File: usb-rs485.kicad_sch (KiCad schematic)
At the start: 4 parts

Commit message: moved it elsewhere but MEH
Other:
- sheet RS485 Transceiver ports: added VLOGIC_MOTOR; removed none
- moved on the sheet: J2
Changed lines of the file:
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@@
+    (stroke (width 0) (type default))
+  )
+  (wire (pts (xy 324.485 145.415) (xy 324.485 146.685))
     (stroke (width 0) (type default))
   )
@@
     (stroke (width 0) (type default))
   )
-  (wire (pts (xy 328.93 154.94) (xy 328.93 155.575))
+  (wire (pts (xy 337.82 154.94) (xy 337.82 155.575))
     (stroke (width 0) (type default))
   )
@@
     (stroke (width 0) (type default))
   )
-  (wire (pts (xy 322.58 149.86) (xy 329.565 149.86))
+  (wire (pts (xy 322.58 149.86) (xy 338.455 149.86))
     (stroke (width 0) (type default))
   )
@@
     (stroke (width 0) (type default))
   )
-  (wire (pts (xy 328.93 147.32) (xy 329.565 147.32))
+  (wire (pts (xy 337.82 147.32) (xy 338.455 147.32))
     (stroke (width 0) (type default))
   )
@@
     (stroke (width 0) (type default))
   )
+  (wire (pts (xy 322.58 152.4) (xy 338.455 152.4))
+    (stroke (width 0) (type default))
+  )
   (wire (pts (xy 300.355 192.405) (xy 302.26 192.405))
     (stroke (width 0) (type default))
@@
     (stroke (width 0) (type default))
   )
-  (wire (pts (xy 322.58 152.4) (xy 329.565 152.4))
-    (stroke (width 0) (type default))
-  )
   (wire (pts (xy 279.4 149.86) (xy 299.085 149.86))
     (stroke (width 0) (type default))
@@
     (stroke (width 0) (type default))
   )
-  (wire (pts (xy 328.93 146.685) (xy 328.93 147.32))
-    (stroke (width 0) (type default))
-  )
-  (wire (pts (xy 328.93 154.94) (xy 329.565 154.94))
+  (wire (pts (xy 324.485 146.685) (xy 322.58 146.685))
+    (stroke (width 0) (type default))
+  )
+  (wire (pts (xy 337.82 146.685) (xy 337.82 147.32))
+    (stroke (width 0) (type default))
+  )
+  (wire (pts (xy 337.82 154.94) (xy 338.455 154.94))
     (stroke (width 0) (type default))
   )
@@
     (effects (font (size 1.27 1.27)) (justify right bottom))
   )
+  (label "6V0" (at 324.485 145.415 0) (fields_autoplaced)
+    (effects (font (size 1.27 1.27)) (justify left bottom))
+  )
   (label "RX" (at 287.02 149.86 0) (fields_autoplaced)
     (effects (font (size 1.27 1.27)) (justify left bottom))
   )
-  (label "VUSB" (at 328.93 146.685 180) (fields_autoplaced)
+  (label "VUSB" (at 337.82 146.685 180) (fields_autoplaced)
     (effects (font (size 1.27 1.27)) (justify right bottom))
   )
@@
     )
   )
-  (symbol (lib_id "power:GND") (at 328.93 155.575 0) (unit 1)
+  (symbol (lib_id "power:GND") (at 337.82 155.575 0) (unit 1)
     (in_bom yes) (on_board yes) (dnp no)
-    (property "Reference" "#PWR011" (at 328.93 161.925 0)
-      (effects (font (size 1.27 1.27)) hide)
-    )
-    (property "Value" "GND" (at 328.93 159.385 0)
-      (effects (font (size 1.27 1.27)))
-    )
-    (property "Footprint" "" (at 328.93 155.575 0)
-      (effects (font (size 1.27 1.27)) hide)
-    )
-    (property "Datasheet" "" (at 328.93 155.575 0)
+    (property "Reference" "#PWR011" (at 337.82 161.925 0)
+      (effects (font (size 1.27 1.27)) hide)
+    )
+    (property "Value" "GND" (at 337.82 159.385 0)
+      (effects (font (size 1.27 1.27)))
+    )
+    (property "Footprint" "" (at 337.82 155.575 0)
+      (effects (font (size 1.27 1.27)) hide)
+    )
+    (property "Datasheet" "" (at 337.82 155.575 0)
       (effects (font (size 1.27 1.27)) hide)
     )
@@
     )
   )
-  (symbol (lib_id "usb-rs485:ThruHoleX4") (at 332.105 151.13 0) (mirror y) (unit 1)
+  (symbol (lib_id "usb-rs485:ThruHoleX4") (at 340.995 151.13 0) (mirror y) (unit 1)
     (in_bom no) (on_board yes) (dnp no) (fields_autoplaced)
-    (property "Reference" "J2" (at 336.55 151.13 0)
-      (effects (font (size 1.27 1.27)) (justify right))
-    )
-    (property "Value" "~" (at 330.835 149.86 0)
-      (effects (font (size 1.27 1.27)))
-    )
-    (property "Footprint" "usb-rs485:ThruHoleBreadboardX4" (at 330.835 149.86 0)
-      (effects (font (size 1.27 1.27)) hide)
-    )
-    (property "Datasheet" "" (at 330.835 149.86 0)
+    (property "Reference" "J2" (at 345.44 151.13 0)
+      (effects (font (size 1.27 1.27)) (justify right))
+    )
+    (property "Value" "~" (at 339.725 149.86 0)
+      (effects (font (size 1.27 1.27)))
+    )
+    (property "Footprint" "usb-rs485:ThruHoleBreadboardX4" (at 339.725 149.86 0)
+      (effects (font (size 1.27 1.27)) hide)
+    )
+    (property "Datasheet" "" (at 339.725 149.86 0)
       (effects (font (size 1.27 1.27)) hide)
     )
@@
       (effects (font (size 1.27 1.27)) (justify right))
     )
+    (pin "VLOGIC_MOTOR" input (at 322.58 146.685 0)
+      (effects (font (size 1.27 1.27)) (justify right))
+    )

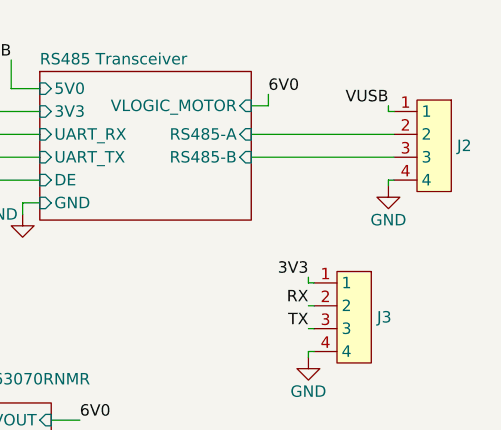
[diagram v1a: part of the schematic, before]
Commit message: routed best placement. Has 6V on the output and on a final header hole for max conveniences
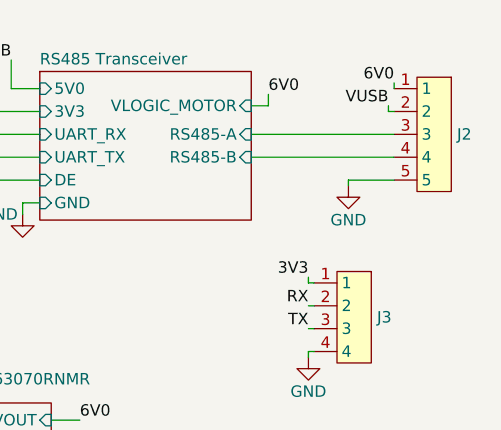
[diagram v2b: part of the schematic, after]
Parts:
- removed J2: ~, usb-rs485:ThruHoleBreadboardX4, symbol usb-rs485:ThruHoleX4
- added J2: ~, usb-rs485:ThruHoleBreadboardX5, symbol usb-rs485:ThruHoleX5
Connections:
- net 6V0: now also J2.1
- net GND: now also J2.5
- net RS485 Transceiver/RS485-A: now also J2.3
- net RS485 Transceiver/RS485-B: now also J2.4
- net VUSB: now also J2.2
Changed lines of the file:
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@@
+    (stroke (width 0) (type default))
+  )
+  (wire (pts (xy 338.455 144.145) (xy 338.455 144.78))
     (stroke (width 0) (type default))
   )
@@
     (stroke (width 0) (type default))
   )
-  (wire (pts (xy 337.82 154.94) (xy 337.82 155.575))
+  (wire (pts (xy 333.375 154.94) (xy 333.375 155.575))
     (stroke (width 0) (type default))
   )
@@
     (stroke (width 0) (type default))
   )
-  (wire (pts (xy 337.82 154.94) (xy 338.455 154.94))
+  (wire (pts (xy 333.375 154.94) (xy 338.455 154.94))
     (stroke (width 0) (type default))
   )
@@
   )
   (label "TX" (at 328.93 171.45 180) (fields_autoplaced)
+    (effects (font (size 1.27 1.27)) (justify right bottom))
+  )
+  (label "6V0" (at 338.455 144.145 180) (fields_autoplaced)
     (effects (font (size 1.27 1.27)) (justify right bottom))
   )
@@
     )
   )
-  (symbol (lib_id "power:GND") (at 337.82 155.575 0) (unit 1)
+  (symbol (lib_id "power:GND") (at 333.375 155.575 0) (unit 1)
     (in_bom yes) (on_board yes) (dnp no)
-    (property "Reference" "#PWR011" (at 337.82 161.925 0)
-      (effects (font (size 1.27 1.27)) hide)
-    )
-    (property "Value" "GND" (at 337.82 159.385 0)
-      (effects (font (size 1.27 1.27)))
-    )
-    (property "Footprint" "" (at 337.82 155.575 0)
-      (effects (font (size 1.27 1.27)) hide)
-    )
-    (property "Datasheet" "" (at 337.82 155.575 0)
+    (property "Reference" "#PWR011" (at 333.375 161.925 0)
+      (effects (font (size 1.27 1.27)) hide)
+    )
+    (property "Value" "GND" (at 333.375 159.385 0)
+      (effects (font (size 1.27 1.27)))
+    )
+    (property "Footprint" "" (at 333.375 155.575 0)
+      (effects (font (size 1.27 1.27)) hide)
+    )
+    (property "Datasheet" "" (at 333.375 155.575 0)
       (effects (font (size 1.27 1.27)) hide)
     )
@@
     )
   )
-  (symbol (lib_id "usb-rs485:ThruHoleX4") (at 340.995 151.13 0) (mirror y) (unit 1)
-    (in_bom no) (on_board yes) (dnp no) (fields_autoplaced)
-    (property "Reference" "J2" (at 345.44 151.13 0)
+  (symbol (lib_id "power:GND") (at 328.93 174.625 0) (unit 1)
+    (in_bom yes) (on_board yes) (dnp no)
+    (property "Reference" "#PWR012" (at 328.93 180.975 0)
+      (effects (font (size 1.27 1.27)) hide)
+    )
+    (property "Value" "GND" (at 328.93 178.435 0)
+      (effects (font (size 1.27 1.27)))
+    )
+    (property "Footprint" "" (at 328.93 174.625 0)
+      (effects (font (size 1.27 1.27)) hide)
+    )
+    (property "Datasheet" "" (at 328.93 174.625 0)
+      (effects (font (size 1.27 1.27)) hide)
+    )
+    (pin "1")
+    (instances
+      (project "usb-rs485"
+        (path "/19e4cb9f-d0a4-4ce0-8aa4-5fe95563dc37"
+          (reference "#PWR012") (unit 1)
+        )
+      )
+    )
+  )
+  (symbol (lib_id "usb-rs485:ThruHoleX5") (at 340.995 148.59 0) (mirror y) (unit 1)
+    (in_bom yes) (on_board yes) (dnp no) (fields_autoplaced)
+    (property "Reference" "J2" (at 345.44 149.86 0)
       (effects (font (size 1.27 1.27)) (justify right))
     )
-    (property "Value" "~" (at 339.725 149.86 0)
-      (effects (font (size 1.27 1.27)))
-    )
-    (property "Footprint" "usb-rs485:ThruHoleBreadboardX4" (at 339.725 149.86 0)
-      (effects (font (size 1.27 1.27)) hide)
-    )
-    (property "Datasheet" "" (at 339.725 149.86 0)
+    (property "Value" "~" (at 339.725 147.32 0)
+      (effects (font (size 1.27 1.27)))
+    )
+    (property "Footprint" "usb-rs485:ThruHoleBreadboardX5" (at 339.725 147.32 0)
+      (effects (font (size 1.27 1.27)) hide)
+    )
+    (property "Datasheet" "" (at 339.725 147.32 0)
       (effects (font (size 1.27 1.27)) hide)
     )
@@
     (pin "2")
     (pin "1")
+    (pin "5")
     (instances
       (project "usb-rs485"
@@
         )
       )
-    )
-  )
-  (symbol (lib_id "power:GND") (at 328.93 174.625 0) (unit 1)
-    (in_bom yes) (on_board yes) (dnp no)
-    (property "Reference" "#PWR012" (at 328.93 180.975 0)
-      (effects (font (size 1.27 1.27)) hide)
-    )
-    (property "Value" "GND" (at 328.93 178.435 0)
-      (effects (font (size 1.27 1.27)))
-    )
-    (property "Footprint" "" (at 328.93 174.625 0)
-      (effects (font (size 1.27 1.27)) hide)
-    )
-    (property "Datasheet" "" (at 328.93 174.625 0)
-      (effects (font (size 1.27 1.27)) hide)
-    )
-    (pin "1")
-    (instances
-      (project "usb-rs485"
-        (path "/19e4cb9f-d0a4-4ce0-8aa4-5fe95563dc37"
-          (reference "#PWR012") (unit 1)
-        )
-      )

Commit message: resistors dialed in
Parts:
- R4: value 470k -> 365k
- R5: value 150k -> 47k
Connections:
- net 6V0 renamed 7V0
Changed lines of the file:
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@@
     (stroke (width 0) (type default))
   )
-  (label "6V0" (at 303.53 181.61 0) (fields_autoplaced)
+  (label "7V0" (at 303.53 181.61 0) (fields_autoplaced)
     (effects (font (size 1.27 1.27)) (justify left bottom))
   )
@@
     (effects (font (size 1.27 1.27)) (justify right bottom))
   )
-  (label "6V0" (at 338.455 144.145 180) (fields_autoplaced)
+  (label "7V0" (at 338.455 144.145 180) (fields_autoplaced)
     (effects (font (size 1.27 1.27)) (justify right bottom))
   )
@@
     (effects (font (size 1.27 1.27)) (justify right bottom))
   )
-  (label "6V0" (at 324.485 145.415 0) (fields_autoplaced)
+  (label "7V0" (at 324.485 145.415 0) (fields_autoplaced)
     (effects (font (size 1.27 1.27)) (justify left bottom))
   )
@@
       (effects (font (size 1.27 1.27)) (justify left))
     )
-    (property "Value" "470k" (at 306.07 199.39 0)
+    (property "Value" "365k" (at 306.07 199.39 0)
       (effects (font (size 1.27 1.27)))
     )
@@
       (effects (font (size 1.27 1.27)) (justify left))
     )
-    (property "Value" "150k" (at 306.07 210.82 0)
-      (effects (font (size 1.27 1.27)))
-    )
+    (property "Value" "47k" (at 306.07 210.82 0)
+      (effects (font (size 1.27 1.27)))
+    )

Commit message: lights
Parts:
- added D6: 150060GS84000, usb-rs485:LED_0603_1608Metric, symbol usb-rs485:LED
- added R10: 470, usb-rs485:R_0402_1005Metric, symbol usb-rs485:Resistor
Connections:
- net 7V0: now also D6.2 (A)
- net GND: now also R10.1
- new net: D6.1 (K), R10.2
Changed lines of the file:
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@@
+    (stroke (width 0) (type default))
+  )
+  (wire (pts (xy 332.74 210.82) (xy 332.74 209.55))
     (stroke (width 0) (type default))
   )
@@
     (stroke (width 0) (type default))
   )
+  (wire (pts (xy 332.74 189.23) (xy 332.74 191.77))
+    (stroke (width 0) (type default))
+  )
   (wire (pts (xy 254.635 160.655) (xy 254.635 163.195))
     (stroke (width 0) (type default))
@@
     (stroke (width 0) (type default))
   )
+  (wire (pts (xy 332.74 199.39) (xy 332.74 201.93))
+    (stroke (width 0) (type default))
+  )
   (label "7V0" (at 303.53 181.61 0) (fields_autoplaced)
     (effects (font (size 1.27 1.27)) (justify left bottom))
@@
   (label "VUSB" (at 337.82 146.685 180) (fields_autoplaced)
     (effects (font (size 1.27 1.27)) (justify right bottom))
+  )
+  (label "7V0" (at 332.74 189.23 0) (fields_autoplaced)
+    (effects (font (size 1.27 1.27)) (justify left bottom))
   )
   (label "3V3" (at 328.93 165.735 180) (fields_autoplaced)
@@
     )
   )
+  (symbol (lib_id "power:GND") (at 332.74 210.82 0) (unit 1)
+    (in_bom yes) (on_board yes) (dnp no)
+    (property "Reference" "#PWR014" (at 332.74 217.17 0)
+      (effects (font (size 1.27 1.27)) hide)
+    )
+    (property "Value" "GND" (at 332.74 214.63 0)
+      (effects (font (size 1.27 1.27)))
+    )
+    (property "Footprint" "" (at 332.74 210.82 0)
+      (effects (font (size 1.27 1.27)) hide)
+    )
+    (property "Datasheet" "" (at 332.74 210.82 0)
+      (effects (font (size 1.27 1.27)) hide)
+    )
+    (pin "1")
+    (instances
+      (project "usb-rs485"
+        (path "/19e4cb9f-d0a4-4ce0-8aa4-5fe95563dc37"
+          (reference "#PWR014") (unit 1)
+        )
+      )
+    )
+  )
+  (symbol (lib_id "usb-rs485:LED") (at 332.74 195.58 90) (unit 1)
+    (in_bom yes) (on_board yes) (dnp no)
+    (property "Reference" "D6" (at 328.295 195.58 90)
+      (effects (font (size 1.27 1.27)) (justify right))
+    )
+    (property "Value" "150060GS84000" (at 316.23 198.12 90)
+      (effects (font (size 1.27 1.27)) (justify right))
+    )
+    (property "Footprint" "usb-rs485:LED_0603_1608Metric" (at 332.74 195.58 0)
+      (effects (font (size 1.27 1.27)) hide)
+    )
+    (property "Datasheet" "https://www.we-online.com/components/products/datasheet/150060GS84000.pdf" (at 332.74 195.58 0)
+      (effects (font (size 1.27 1.27)) hide)
+    )
+    (pin "1")
+    (pin "2")
+    (instances
+      (project "usb-rs485"
+        (path "/19e4cb9f-d0a4-4ce0-8aa4-5fe95563dc37"
+          (reference "D6") (unit 1)
+        )
+      )
+    )
+  )
   (symbol (lib_id "usb-rs485:ThruHoleX5") (at 340.995 148.59 0) (mirror y) (unit 1)
     (in_bom yes) (on_board yes) (dnp no) (fields_autoplaced)
@@
         )
       )
+    )
+  )
+  (symbol (lib_id "usb-rs485:Resistor") (at 332.74 205.74 180) (unit 1)
+    (in_bom yes) (on_board yes) (dnp no) (fields_autoplaced)
+    (property "Reference" "R10" (at 330.2 205.105 0)
+      (effects (font (size 1.27 1.27)) (justify left))
+    )
+    (property "Value" "470" (at 335.28 205.74 90)
+      (effects (font (size 1.27 1.27)) hide)
+    )
+    (property "Footprint" "usb-rs485:R_0402_1005Metric" (at 337.82 218.44 0)
+      (effects (font (size 1.27 1.27)) hide)
+    )
+    (property "Datasheet" "~" (at 332.74 205.74 0)
+      (effects (font (size 1.27 1.27)) hide)
+    )
+    (pin "1")
+    (pin "2")
+    (instances
+      (project "usb-rs485"
+        (path "/19e4cb9f-d0a4-4ce0-8aa4-5fe95563dc37"
+          (reference "R10") (unit 1)
+        )
+      )

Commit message: bom callouts no copper change
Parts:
- J2: now left out of the parts list
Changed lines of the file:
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@@
   )
   (symbol (lib_id "usb-rs485:ThruHoleX5") (at 340.995 148.59 0) (mirror y) (unit 1)
-    (in_bom yes) (on_board yes) (dnp no) (fields_autoplaced)
+    (in_bom no) (on_board yes) (dnp no) (fields_autoplaced)
     (property "Reference" "J2" (at 345.44 149.86 0)
       (effects (font (size 1.27 1.27)) (justify right))
